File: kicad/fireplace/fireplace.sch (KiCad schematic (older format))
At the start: 20 parts, among them SW1 SW_Push, SW2 SW_Push, SW3 SW_Push, SW4 SW_Push, U1 ULN2003A, U2 PIC16F84-XX/P, U3 MOC3021M, U4 ATMEGA8-16AU, U5 QSE159, Y1 4MHz

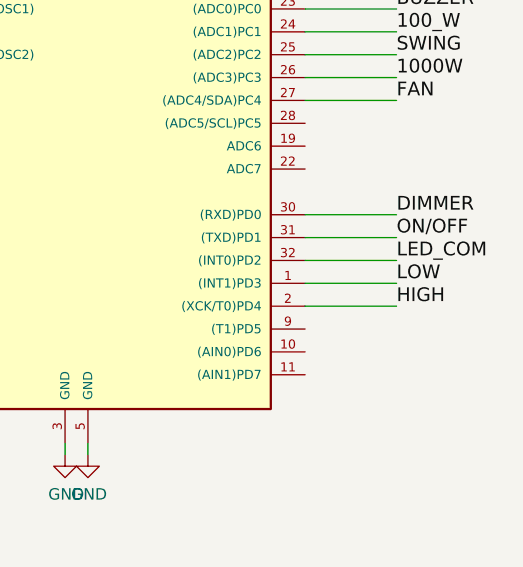
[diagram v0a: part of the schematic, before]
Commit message: Set int0 to ir pin
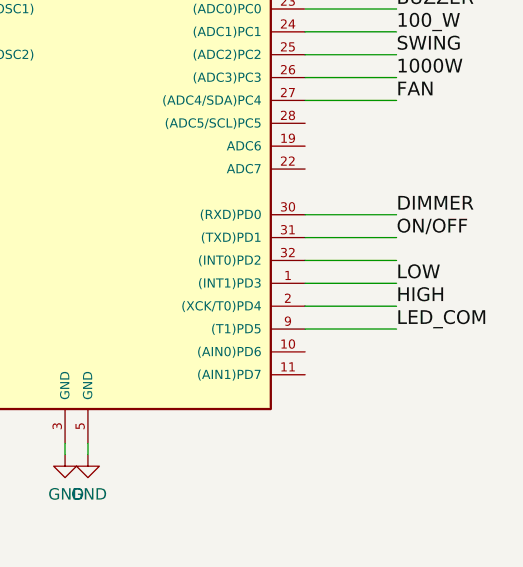
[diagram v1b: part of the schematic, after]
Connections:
- net LED_COM: now also U4.9 ((T1)PD5); no longer U4.32 ((INT0)PD2)
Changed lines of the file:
@@
 Text Label 2100 4350 0    60   ~ 0
-LED_COM
-Text Label 10500 4900 0    60   ~ 0
 LED_COM
 Text Label 10500 5000 0    60   ~ 0
@@
 Text Label 10500 4200 0    60   ~ 0
 FAN
+Wire Wire Line
+	10100 5200 10500 5200
+Text Label 10500 5200 0    60   ~ 0
+LED_COM
 $EndSCHEMATC

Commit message: Good IR work
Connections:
- net IR_IN: now reaches U2.13 (RB7), U5.2 (Out)
- net IR_IN: now also U4.32 ((INT0)PD2)
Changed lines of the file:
@@
 Text Label 10500 5200 0    60   ~ 0
 LED_COM
+Text Label 4900 4450 0    60   ~ 0
+IR_IN
+Text Label 10500 4900 0    60   ~ 0
+IR_IN
 $EndSCHEMATC

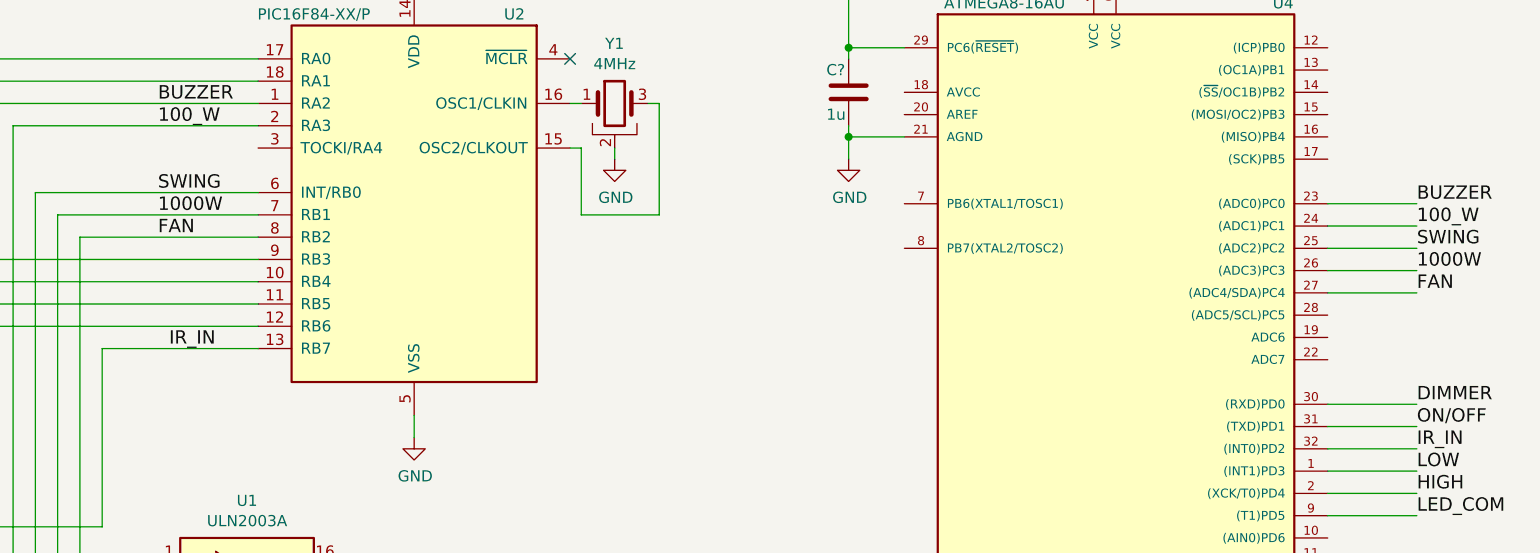
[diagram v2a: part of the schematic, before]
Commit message: Add buzzer, out controll
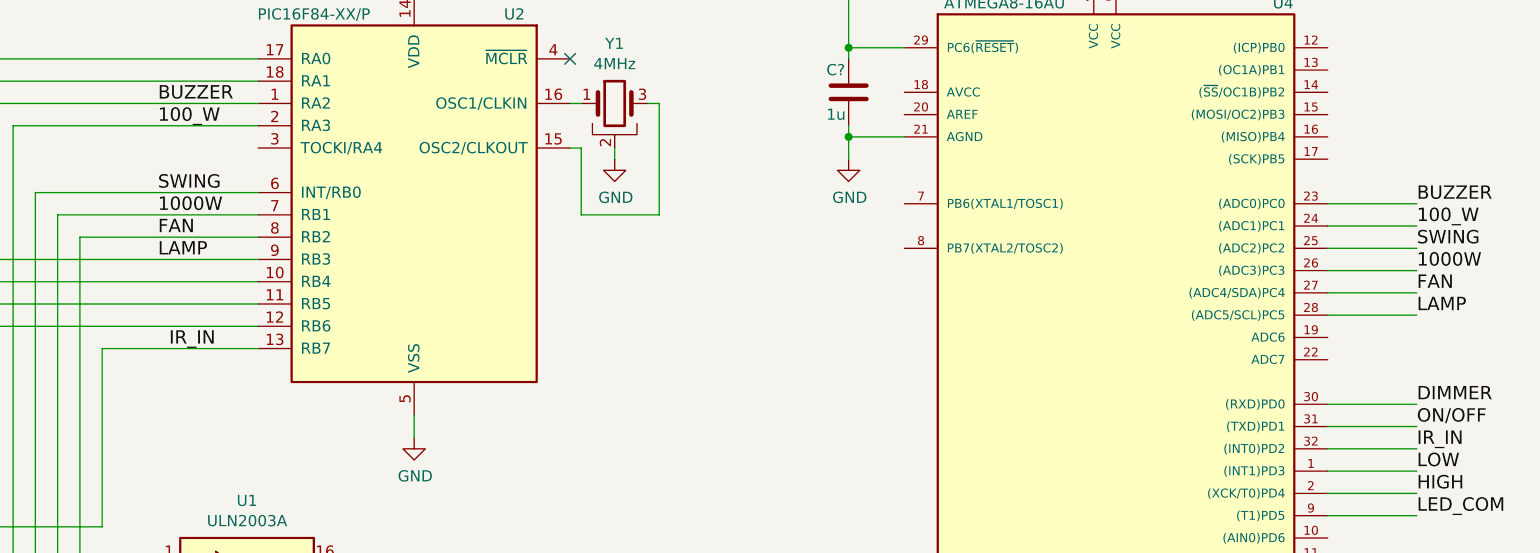
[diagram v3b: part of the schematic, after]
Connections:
- net LAMP: now reaches R3.1, U2.9 (RB3)
- net LAMP: now also U4.28 ((ADC5/SCL)PC5)
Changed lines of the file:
@@
 Text Label 10500 4900 0    60   ~ 0
 IR_IN
+Text Label 4850 4050 0    60   ~ 0
+LAMP
+Wire Wire Line
+	10100 4300 10500 4300
+Text Label 10500 4300 0    60   ~ 0
+LAMP
 $EndSCHEMATC
